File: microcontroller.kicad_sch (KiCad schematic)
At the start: 27 parts, among them J18 Conn_01x06, SW1 SW_Push, U1 STM32F103C8Tx, U2 TPS7B88, U3 MCP1700x-330xxMB, Y1 8M

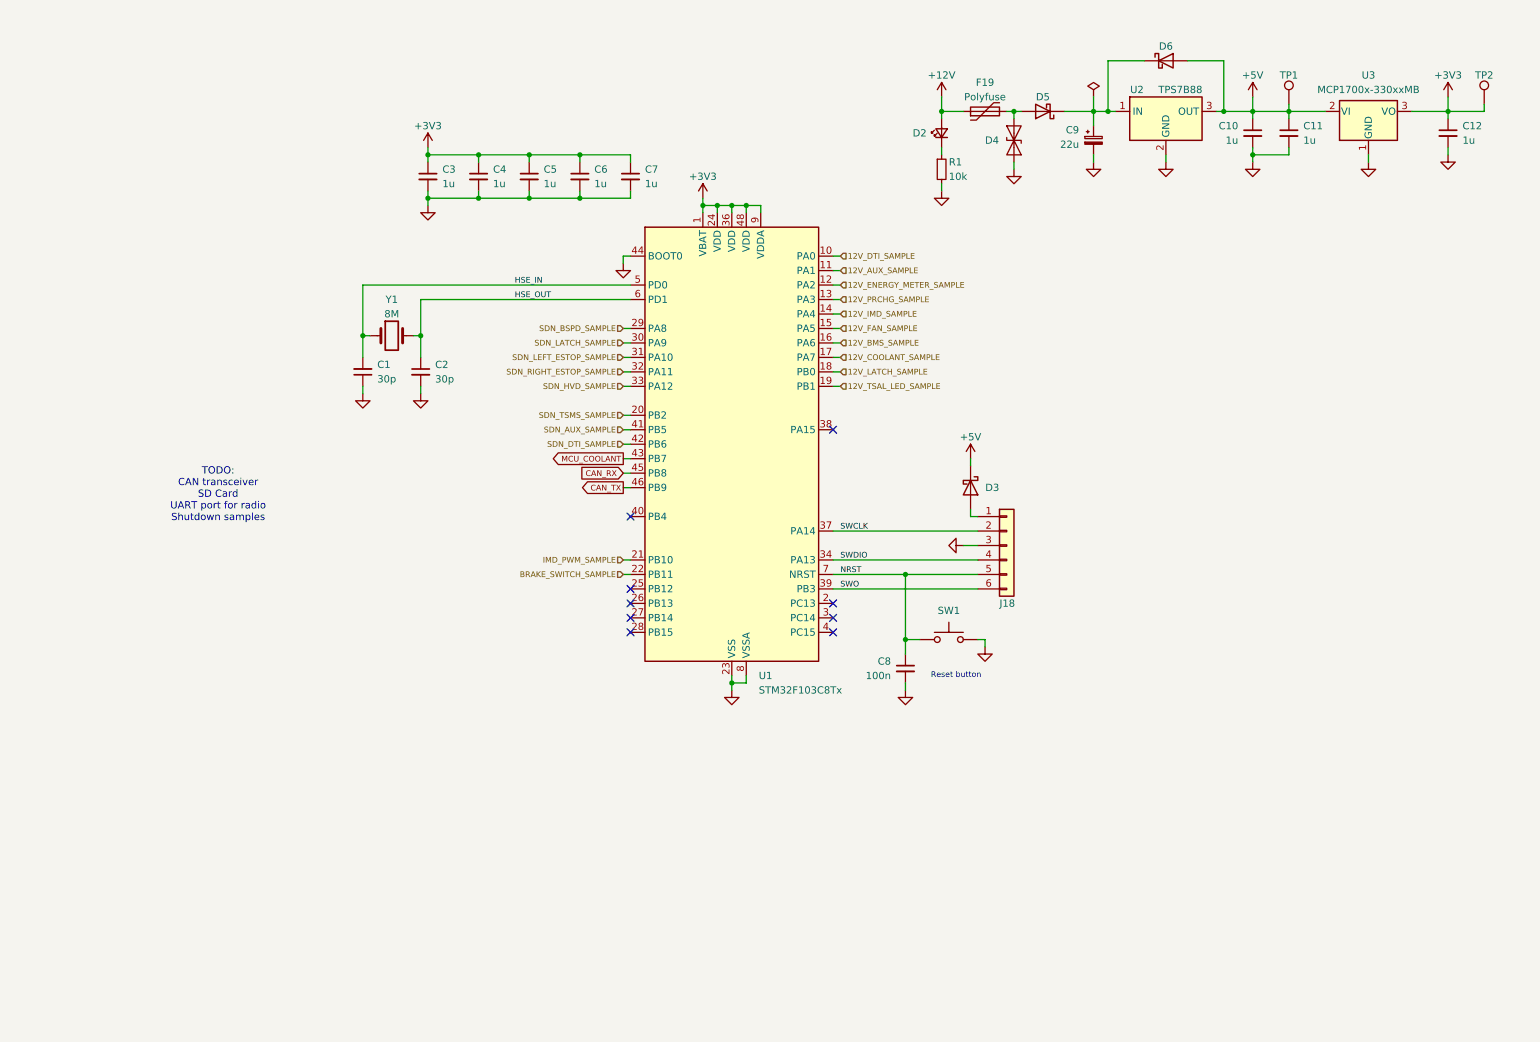
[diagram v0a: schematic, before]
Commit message: schematic: Tentatively finish major schematic parts
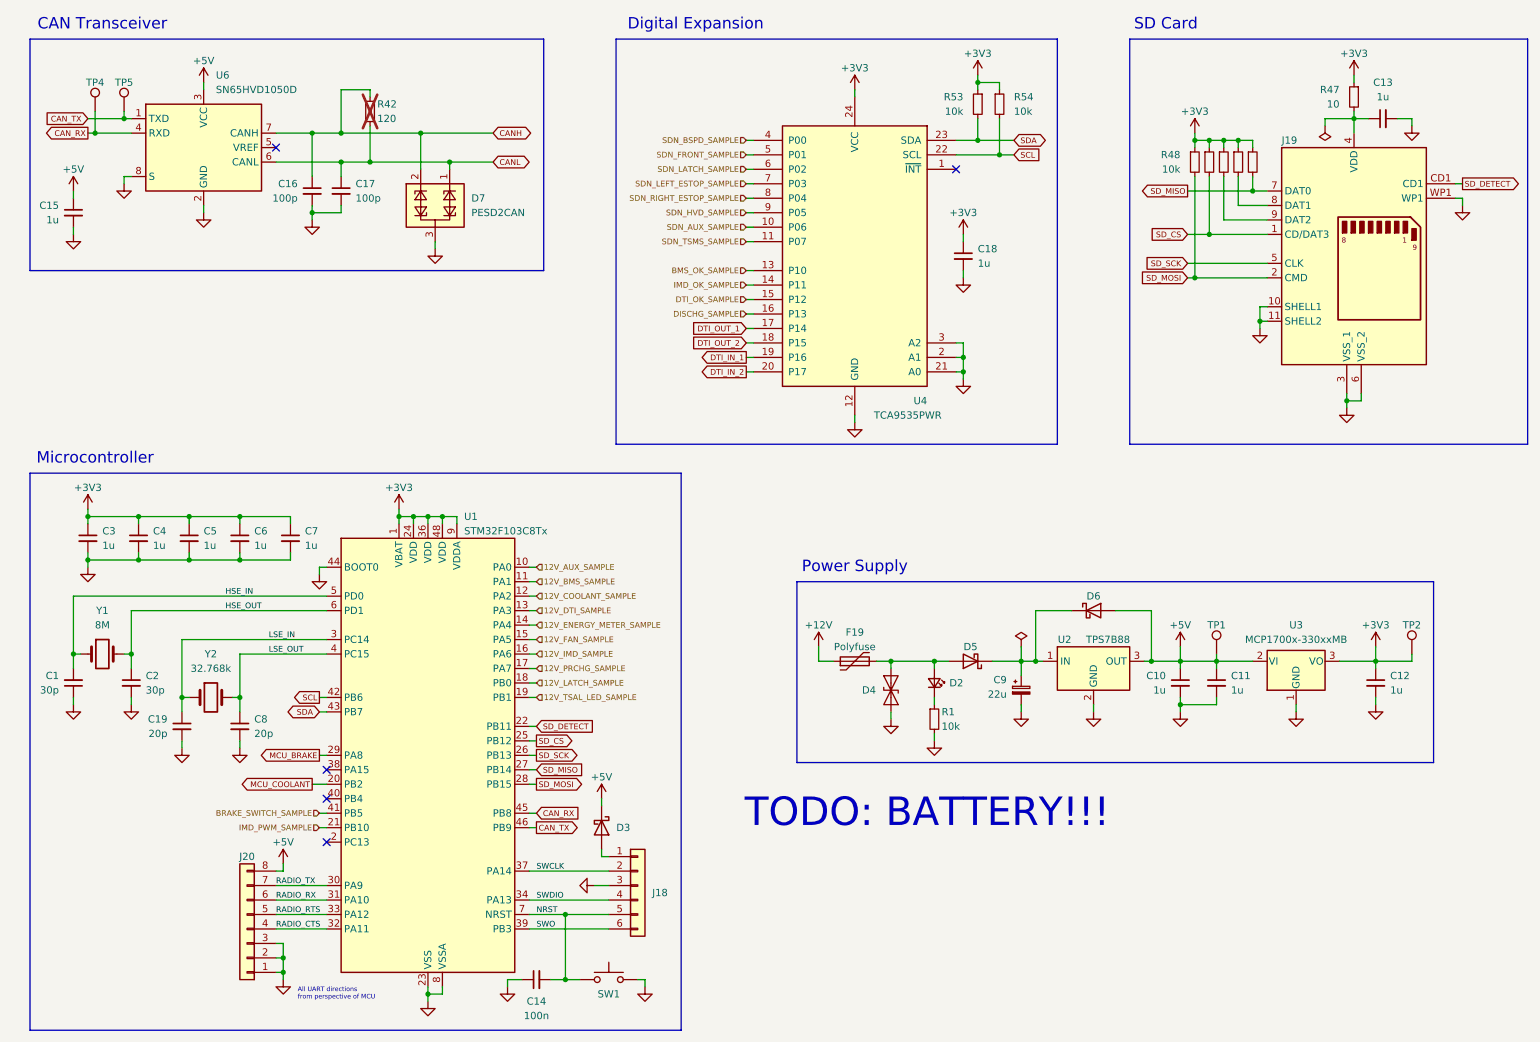
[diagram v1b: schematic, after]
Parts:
- added C13: 1u, symbol Device:C_Small
- added C14: 100n, symbol Device:C_Small
- added C15, C18: 1u, Capacitor_SMD:C_0603_1608Metric, symbol Device:C_Small
- added C16, C17: 100p, Capacitor_SMD:C_0603_1608Metric, symbol Device:C_Small
- added C19: 20p, Capacitor_SMD:C_0603_1608Metric, symbol Device:C_Small
- added D7: PESD2CAN, Package_TO_SOT_SMD:SOT-23, symbol yfs:PESD2CAN
- added J19: 10067847-001RLF, symbol yfs:10067847-001RLF
- added J20: Conn_01x08, symbol Connector_Generic:Conn_01x08
- added R42: 120, Resistor_SMD:R_0603_1608Metric, symbol Device:R_Small
- added R47: 10, symbol Device:R_Small
- added R48, R49, R50, R51, R52, R53, R54: 10k, symbol Device:R_Small
- added TP4, TP5: TestPoint, TestPoint:TestPoint_Keystone_5000-5004_Miniature, symbol Connector:TestPoint
- added U4: TCA9535PWR, Package_SO:TSSOP-24_4.4x7.8mm_P0.65mm, symbol Interface_Expansion:TCA9535PWR
- added U6: SN65HVD1050D, Package_SO:SOIC-8_3.9x4.9mm_P1.27mm, symbol Interface_CAN_LIN:SN65HVD1050D
- added Y2: 32.768k, Crystal:Crystal_SMD_G8-2Pin_3.2x1.5mm, symbol Device:Crystal
- C8: value 100n -> 20p; DigiKey # 1276-1000-1-ND -> (none); LCSC # C1591 -> (none); Mfr Samsung -> (none); Mfr # CL10B104KB8NNNC -> (none); Mouser # 187-CL10B104KB8NNNC -> (none)
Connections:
- net +12V: no longer D2.2 (A)
- net +3V3: now also C18.1, R47.1, R48.1, R49.1, R50.1, R51.1, R52.1, R53.1, R54.1, U4.24 (VCC)
- net +5V: now also C15.1, J20.8 (Pin_8), U6.3 (VCC)
- net 12V_AUX_SAMPLE: now also U1.10 (PA0); no longer U1.11 (PA1)
- net 12V_BMS_SAMPLE: now also U1.11 (PA1); no longer U1.16 (PA6)
- net 12V_COOLANT_SAMPLE: now also U1.12 (PA2); no longer U1.17 (PA7)
- net 12V_DTI_SAMPLE: now also U1.13 (PA3); no longer U1.10 (PA0)
- net 12V_ENERGY_METER_SAMPLE: now also U1.14 (PA4); no longer U1.12 (PA2)
- net 12V_IMD_SAMPLE: now also U1.16 (PA6); no longer U1.14 (PA4)
- net 12V_PRCHG_SAMPLE: now also U1.17 (PA7); no longer U1.13 (PA3)
- net BRAKE_SWITCH_SAMPLE: now also U1.41 (PB5); no longer U1.22 (PB11)
- net CAN_RX: now also TP4.1, U6.4 (RXD)
- net CAN_TX: now also TP5.1, U6.1 (TXD)
- net GND: now also C13.2, C14.1, C15.2, C16.2, C17.2, C18.2, C19.2, D7.3 (CC), J19.10 (SHELL1), J19.11 (SHELL2), J19.3 (VSS_1), J19.6 (VSS_2), J19.WP1, J20.1 (Pin_1), J20.2 (Pin_2), J20.3 (Pin_3), U4.12 (GND), U4.2 (A1), U4.21 (A0), U4.3 (A2), U6.2 (GND), U6.8 (S)
- net MCU_COOLANT: now also U1.20 (PB2); no longer U1.43 (PB7)
- net NRST: now also C14.2; no longer C8.1
- net SDN_AUX_SAMPLE: now also U4.10 (P06); no longer U1.41 (PB5)
- net SDN_BSPD_SAMPLE: now also U4.4 (P00); no longer U1.29 (PA8)
- net SDN_HVD_SAMPLE: now also U4.9 (P05); no longer U1.33 (PA12)
- net SDN_LATCH_SAMPLE: now also U4.6 (P02); no longer U1.30 (PA9)
- net SDN_LEFT_ESTOP_SAMPLE: now also U4.7 (P03); no longer U1.31 (PA10)
- net SDN_RIGHT_ESTOP_SAMPLE: now also U4.8 (P04); no longer U1.32 (PA11)
- net SDN_TSMS_SAMPLE: now also U4.11 (P07); no longer U1.20 (PB2)
- net at D4.2 (A2), D5.2 (A), F19.2: now also D2.2 (A)
- net SD_CS: now reaches U1.25 (PB12)
- net SD_CS: now also J19.1 (CD/DAT3), R49.2
- net SD_SCK: now reaches U1.26 (PB13)
- net SD_SCK: now also J19.5 (CLK)
- net SD_MISO: now reaches U1.27 (PB14)
- net SD_MISO: now also J19.7 (DAT0), R52.2
- net SD_MOSI: now reaches U1.28 (PB15)
- net SD_MOSI: now also J19.2 (CMD), R48.2
- net LSE_IN: now reaches U1.3 (PC14)
- net LSE_IN: now also C19.1, Y2.1
- net LSE_OUT: now reaches U1.4 (PC15)
- net LSE_OUT: now also C8.1, Y2.2
- net SDN_DTI_SAMPLE renamed SCL
- net SCL: now also R54.2, U4.22 (SCL)
- new net: C13.1, J19.4 (VDD), R47.2
- new net: J19.8 (DAT1), R51.2
- new net: J19.9 (DAT2), R50.2
- new net BMS_OK_SAMPLE: U4.13 (P10)
- new net CANH: C16.1, D7.2 (C2), R42.1, U6.7 (CANH)
- new net CANL: C17.1, D7.1 (C1), R42.2, U6.6 (CANL)
- new net DISCHG_SAMPLE: U4.16 (P13)
- new net DTI_IN_1: U4.19 (P16)
- new net DTI_IN_2: U4.20 (P17)
- new net DTI_OK_SAMPLE: U4.15 (P12)
- new net DTI_OUT_1: U4.17 (P14)
- new net DTI_OUT_2: U4.18 (P15)
- new net IMD_OK_SAMPLE: U4.14 (P11)
- new net MCU_BRAKE: U1.29 (PA8)
- new net RADIO_CTS: J20.4 (Pin_4), U1.32 (PA11)
- new net RADIO_RTS: J20.5 (Pin_5), U1.33 (PA12)
- new net RADIO_RX: J20.6 (Pin_6), U1.31 (PA10)
- new net RADIO_TX: J20.7 (Pin_7), U1.30 (PA9)
- new net SDA: R53.2, U1.43 (PB7), U4.23 (SDA)
- new net SDN_FRONT_SAMPLE: U4.5 (P01)
- new net SD_DETECT: J19.CD1, U1.22 (PB11)
- no-connect marks 9 -> 5
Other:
- note added: "All UART directions from perspective of MCU"
- note added: "CAN Transceiver"
- note added: "Digital Expansion"
- note added: "Microcontroller"
- note added: "Power Supply"
- note added: "SD Card"
- note added: "TODO: BATTERY!!!"
- note removed: "Reset button"
- note removed: "TODO: CAN transceiver SD Card UART port for radio Shutdown samples"
- company: (none) -> York Formula Student
- title: (none) -> Rear Distribution
- moved on the sheet: C1, C10, C11, C12, C2, C3, C4, C5, C6, C7, C9, D2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

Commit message: schematic: Re-annotate and add RTC battery
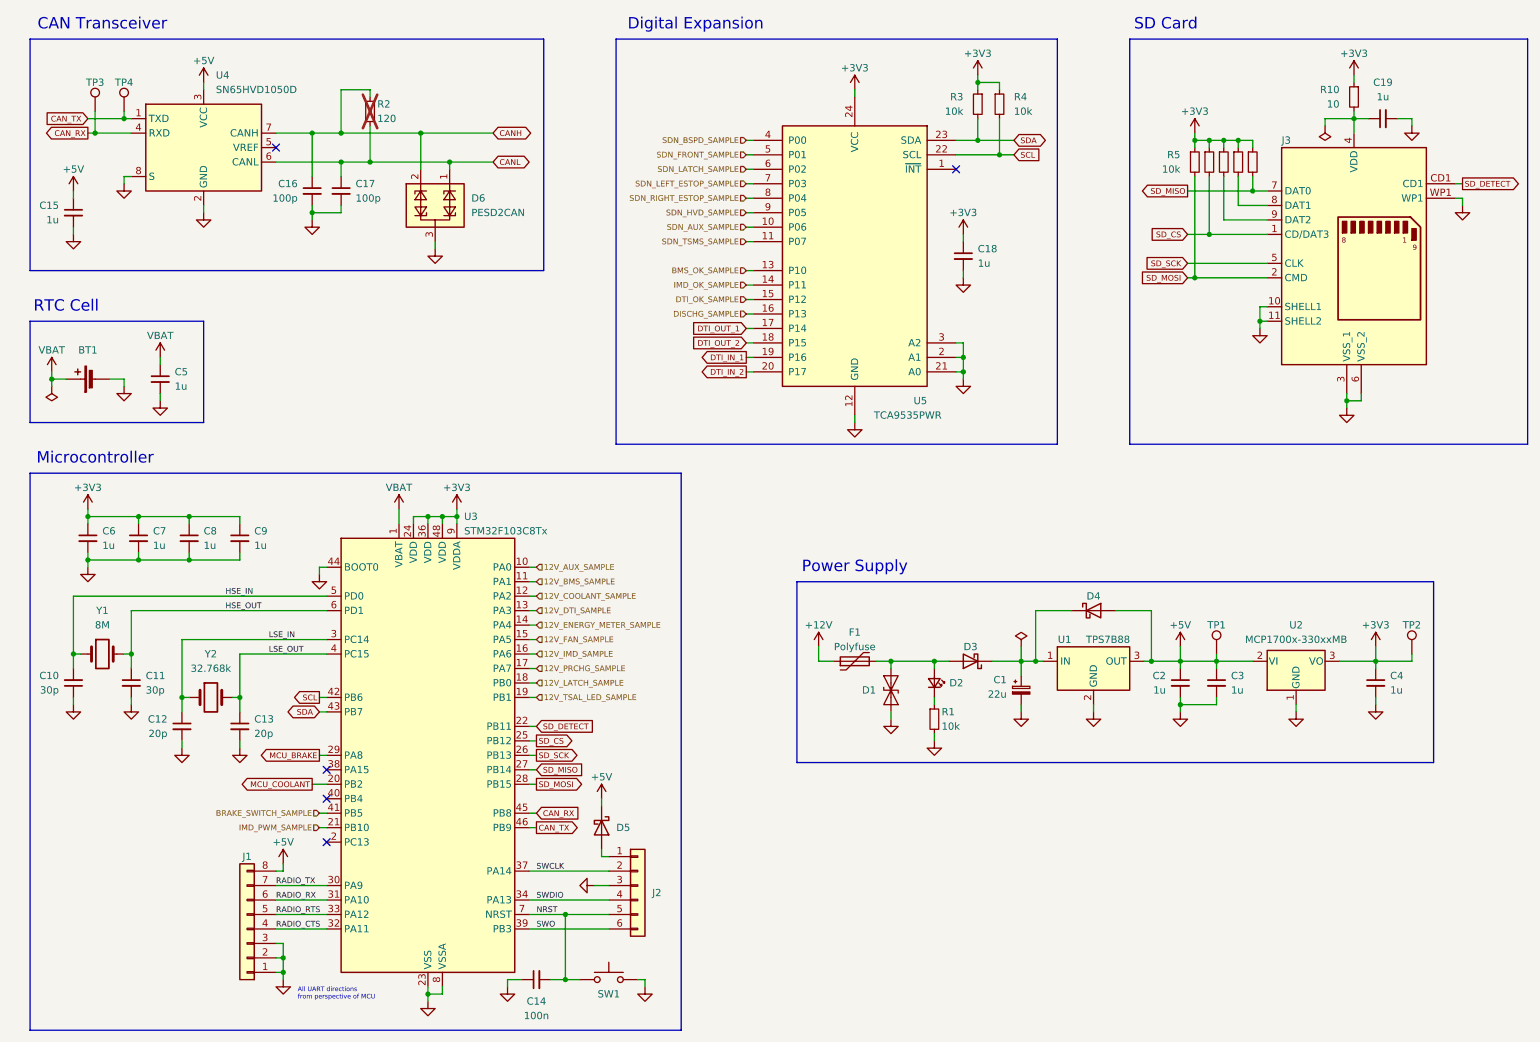
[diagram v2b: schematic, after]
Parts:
- removed C7: 1u, Capacitor_SMD:C_0603_1608Metric, symbol Device:C_Small
- added BT1: Battery_Cell, symbol Device:Battery_Cell
- added C5: 1u, Capacitor_SMD:C_0603_1608Metric, symbol Device:C_Small
- renumbered C9 to C1, C1 to C10, C2 to C11, C19 to C12, C8 to C13, C13 to C19, C10 to C2, C11 to C3, C12 to C4, C3 to C6, C4 to C7, C5 to C8, C6 to C9, D4 to D1, D5 to D3, D6 to D4, D3 to D5, D7 to D6, F19 to F1, J20 to J1, J18 to J2, J19 to J3, R47 to R10, R42 to R2, R53 to R3, R54 to R4, R48 to R5, R49 to R6, R50 to R7, R51 to R8, R52 to R9, TP4 to TP3, TP5 to TP4, U2 to U1, U3 to U2, U1 to U3, U6 to U4, U4 to U5
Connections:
- net +3V3: no longer U3.1 (VBAT)
- net GND: now also BT1.2 (-), C5.2
- new net VBAT: BT1.1 (+), C5.1, U3.1 (VBAT)
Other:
- note added: "RTC Cell"
- note removed: "TODO: BATTERY!!!"

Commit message: schematic: Assign footprints and fill most of BOM
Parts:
- BT1: footprint (none) -> yfs:BAT-SMD_BS-CR2032-8
- C14: footprint (none) -> Capacitor_SMD:C_0603_1608Metric; DigiKey # (none) -> 1276-1000-1-ND; LCSC # (none) -> C1591; Mfr (none) -> Samsung; Mfr # (none) -> CL10B104KB8NNNC; Mouser # (none) -> 187-CL10B104KB8NNNC
- C15: Dist LCSC -> (none); Dist # C5199872 -> (none); LCSC # (none) -> C5199872; Mouser # (none) -> 187-CL10B105KB8NQNC
- C16, C17: DigiKey # (none) -> 490-4771-1-ND; Dist LCSC -> (none); Dist # C126576 -> (none); LCSC # (none) -> C126576; Mouser # (none) -> 81-GCM1885C2A101JA6D
- C19: footprint (none) -> Capacitor_SMD:C_0603_1608Metric; DigiKey # (none) -> 490-GQM1875C2E300GB12DCT-ND; LCSC # (none) -> C5199872; Mfr (none) -> Samsung; Mfr # (none) -> CL10B105KB8NQNC; Mouser # (none) -> 187-CL10B105KB8NQNC
- D6: DigiKey # (none) -> 1727-3891-1-ND; Dist LCSC -> (none); Dist # C75176 -> (none); LCSC # (none) -> C75176; Mouser # (none) -> 771-PESD2CAN-T/R
- J1: footprint (none) -> yfs:MolexMicrofitPlus1x8; DigiKey # (none) -> 900-2157601008-ND; Mfr (none) -> Molex; Mfr # (none) -> 2157601008; Mouser # (none) -> 538-215760-1008
- J3: footprint (none) -> yfs:10067847-001RLF_AMP
- R10: footprint (none) -> Resistor_SMD:R_0603_1608Metric
- R3, R4, R5, R6, R7, R8, R9: footprint (none) -> Resistor_SMD:R_0603_1608Metric; LCSC # (none) -> C25804; Mfr (none) -> Uni-Royal; Mfr # (none) -> 0603WAF1002T5E
- TP3, TP4: DigiKey # (none) -> 36-5000-ND; LCSC # (none) -> C5199900; Mfr (none) -> Keystone Electronics; Mfr # (none) -> 5000; Mouser # (none) -> 534-5000
- U4: DigiKey # (none) -> 296-26335-1-ND; Dist LCSC -> (none); Dist # C14019 -> (none); LCSC # (none) -> C14019; Mouser # (none) -> 595-SN65HVD1050DR

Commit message: *: Setup PCB
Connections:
- net SD_VCC: now reaches C19.1, J3.4 (VDD), R10.2
- net SD_DAT1: now reaches J3.8 (DAT1), R8.2
- net SD_DAT2: now reaches J3.9 (DAT2), R7.2
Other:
- moved on the sheet: R5

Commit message: pcb: Add layout progress so far
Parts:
- removed J1: Conn_01x08, yfs:MolexMicrofitPlus1x8, symbol Connector_Generic:Conn_01x08
- added J1: Conn_01x06, yfs:MolexMicrofitPlus2x3, symbol Connector_Generic:Conn_01x06
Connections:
- net 12V_AUX_SAMPLE is gone; now on net 12V_BMS_SAMPLE: U3.10 (PA0)
- net DTI_OUT_1 is gone; now on net MCU_BRAKE: U5.17 (P14)
- net +5V: now also J1.2 (Pin_2)
- net 12V_BMS_SAMPLE: no longer U3.11 (PA1)
- net 12V_COOLANT_SAMPLE: now also U3.14 (PA4); no longer U3.12 (PA2)
- net 12V_DTI_SAMPLE: now also U3.17 (PA7); no longer U3.13 (PA3)
- net 12V_ENERGY_METER_SAMPLE: now also U3.19 (PB1); no longer U3.14 (PA4)
- net 12V_FAN_SAMPLE: now also U3.12 (PA2); no longer U3.15 (PA5)
- net 12V_IMD_SAMPLE: now also U3.11 (PA1); no longer U3.16 (PA6)
- net 12V_PRCHG_SAMPLE: now also U3.13 (PA3); no longer U3.17 (PA7)
- net 12V_TSAL_LED_SAMPLE: now also U3.16 (PA6); no longer U3.19 (PB1)
- net BMS_OK_SAMPLE: now also U5.15 (P12); no longer U5.13 (P10)
- net BRAKE_SWITCH_SAMPLE: now also U3.21 (PB10); no longer U3.41 (PB5)
- net DISCHG_SAMPLE: now also U5.14 (P11); no longer U5.16 (P13)
- net DTI_OK_SAMPLE: now also U3.20 (PB2); no longer U5.15 (P12)
- net GND: now also J1.1 (Pin_1)
- net IMD_OK_SAMPLE: now also U5.16 (P13); no longer U5.14 (P11)
- net IMD_PWM_SAMPLE: now also U3.41 (PB5); no longer U3.21 (PB10)
- net MCU_BRAKE: no longer U3.29 (PA8)
- net MCU_COOLANT: now also U5.13 (P10); no longer U3.20 (PB2)
- net RADIO_CTS: now also J1.5 (Pin_5)
- net RADIO_RTS: now also J1.4 (Pin_4)
- net RADIO_RX: now also J1.6 (Pin_6)
- net RADIO_TX: now also J1.3 (Pin_3)
- net SDN_AUX_SAMPLE: now also U5.7 (P03); no longer U5.10 (P06)
- net SDN_BSPD_SAMPLE: now also U5.9 (P05); no longer U5.4 (P00)
- net SDN_FRONT_SAMPLE: now also U5.6 (P02); no longer U5.5 (P01)
- net SDN_HVD_SAMPLE: now also U5.11 (P07); no longer U5.9 (P05)
- net SDN_LATCH_SAMPLE: now also U5.5 (P01); no longer U5.6 (P02)
- net SDN_LEFT_ESTOP_SAMPLE: now also U5.4 (P00); no longer U5.7 (P03)
- net SDN_RIGHT_ESTOP_SAMPLE: now also U5.10 (P06); no longer U5.8 (P04)
- net SDN_TSMS_SAMPLE: now also U5.8 (P04); no longer U5.11 (P07)
- net SD_DETECT: now also U3.29 (PA8); no longer U3.22 (PB11)
- net 12V_SAFE: now reaches C1.1, D3.1 (K), D4.1 (K), U1.1 (IN)
- net 12V_FUSED: now reaches D1.2 (A2), D2.2 (A), D3.2 (A), F1.2
- net DTI_IN_1: no longer names the net of U5.19 (P16)
- net DTI_IN_2: no longer names the net of U5.20 (P17)
- net DTI_OUT_2: no longer names the net of U5.18 (P15)
- new net 12V_BRAKE_LIGHT_SAMPLE: U3.15 (PA5)
- no-connect marks 5 -> 9
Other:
- note added: "TODO: LEDS"
- moved on the sheet: D5, J2

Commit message: *: Tentatively finish everything
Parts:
- removed J3: 10067847-001RLF, yfs:10067847-001RLF_AMP, symbol yfs:10067847-001RLF
- removed TP3, TP4: TestPoint, TestPoint:TestPoint_Keystone_5000-5004_Miniature, symbol Connector:TestPoint
- added J3: 47219-2001, yfs:Molex_SD_Slot_47219-2001, symbol yfs:Molex_SD_Slot_47219-2001
- R6: now not fitted
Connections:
- net GND: now also J3.6 (VSS), J3.G1, J3.G2, J3.G3, J3.G4
- net SD_CS: now also J3.2 (CD/DAT3)
- net SD_DAT1: now also J3.8 (DAT1)
- net SD_DAT2: now also J3.1 (DAT2)
- net SD_MISO: now also J3.7 (DAT0)
- net SD_MOSI: now also J3.3 (CMD)
- net SD_SCK: now also J3.5 (CLK)
- net SD_VCC: now also J3.4 (VDD)
- net SD_DETECT: no longer names the net of U3.29 (PA8)
- no-connect marks 9 -> 10

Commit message: pcb: Add model for 2x3 MF+ and fix fuse model alignment
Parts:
- J1: Mfr (none) -> Molex; Mfr # (none) -> 2125280600
- J3: Mfr (none) -> Molex; Mfr # (none) -> 472192001
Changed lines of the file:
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@@
+			)
+		)
+		(property "Mfr" "Molex"
+			(at 54.61 173.99 0)
+			(effects
+				(font
+					(size 1.27 1.27)
+				)
+				(hide yes)
+			)
+		)
+		(property "Mfr #" "2125280600"
+			(at 54.61 173.99 0)
+			(effects
+				(font
+					(size 1.27 1.27)
+				)
+				(hide yes)
 			)
 		)
@@
 			(at 236.22 39.37 0)
 			(effects
+				(font
+					(size 1.27 1.27)
+				)
+				(hide yes)
+			)
+		)
+		(property "Mfr" "Molex"
+			(at 236.22 39.37 0)
+			(effects
+				(font
+					(size 1.27 1.27)
+				)
+				(hide yes)
+			)
+		)
+		(property "Mfr #" "472192001"
+			(at 236.22 39.37 0)
+			(effects
